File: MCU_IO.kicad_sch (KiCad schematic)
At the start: 44 parts, among them J15 Conn_01x02, Q1 IRLML2803, SW1 B3FS-1002P, SW2 B3FS-1002P, U1 RP235x-B, U2 MAX706RESA+, U3 MR25H40MDF, Y1 12MHz

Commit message: Addressed design issues
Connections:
- net Payload_EN: now also U1.37 (GPIO29); no longer U1.38 (GPIO30)
- net Payload_FLT: now also U1.38 (GPIO30); no longer U1.37 (GPIO29)

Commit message: v4.0 Updates
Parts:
- removed J15: Conn_01x02, Connector_PinHeader_2.54mm:PinHeader_1x02_P2.54mm_Vertical, symbol Connector_Generic:Conn_01x02
- added R13, R14, R15, R16: 100k, Resistor_SMD:R_0603_1608Metric, symbol Device:R_Small
- added TP1, TP2: TestPoint, TestPoint:TestPoint_Pad_D1.5mm, symbol Connector:TestPoint
- Y1: value 12MHz -> ABM8-272-T3; Part ABM8-272-T3 -> 12MHz
- renumbered D12 to D1, L4 to L1, R8 to R10, R9 to R11, R10 to R12, R162 to R5, R5 to R6, R163 to R7, R6 to R8, R7 to R9
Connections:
- net COIL_EN: now also R13.1
- net GND: now also R13.2, R14.2, R15.2, R16.2
- net HEATER_ENABLE: now also R14.1
- net Jetson_EN: now also R15.1
- net RW_EN: now also R16.1
- net SWCLK: now also TP2.1
- net SWDIO: now also TP1.1
- net Payload_CSn: no longer names the net of U1.36 (GPIO28)
- net Payload_EN: no longer names the net of U1.37 (GPIO29)
- net Payload_FLT: no longer names the net of U1.38 (GPIO30)
- net Payload_IO0: no longer names the net of U1.18 (GPIO18)
- net Payload_IO1: no longer names the net of U1.17 (GPIO17)
- net Payload_IO2: no longer names the net of U1.16 (GPIO16)
- no-connect marks 6 -> 12
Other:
- moved on the sheet: C10, C21, C22, L1, Q1, R10, R11, R12, R8, R9, SW1, SW2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

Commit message: DFM updates
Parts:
- C1, C14, C15, C16, C19, C2, C20, C22, C3, C4, C5, C6, C7, C8, C9: MPN (none) -> C307348
- C10: MPN (none) -> C16193991
- C11, C12: MPN (none) -> C3861036
- C13: MPN (none) -> C386084
- C17, C18: MPN (none) -> C346205
- C21: MPN (none) -> C2214844
- D1: Flight WS2812B-B -> (none); MPN (none) -> C2890040; Manufacturer_Name Worldsemi -> (none); Manufacturer_Part_Number WS2812B-B -> (none); Proto WS2812B-B -> (none)
- L1: MPN (none) -> C42411119; Part AOTA-B201610S3R3-101-T -> (none)
- Q1: MPN (none) -> C2590
- R1: MPN (none) -> C844757
- R10, R11, R7: MPN (none) -> C2479067
- R12, R5: MPN (none) -> C2484712
- R13, R14, R15, R16, R9: MPN (none) -> C237792
- R2: MPN (none) -> C3029194
- R3, R4: MPN (none) -> C844545
- R6: MPN (none) -> C844915
- R8: DNI (none) -> DNI; now left out of the parts list
- SW1, SW2: value B3FS-1002P -> B3U-1000P; MPN (none) -> C231329
- TP1, TP2: now left out of the parts list
- U1: MPN (none) -> C42415655
- U2: MPN (none) -> C28380
- Y1: MPN (none) -> C20625731

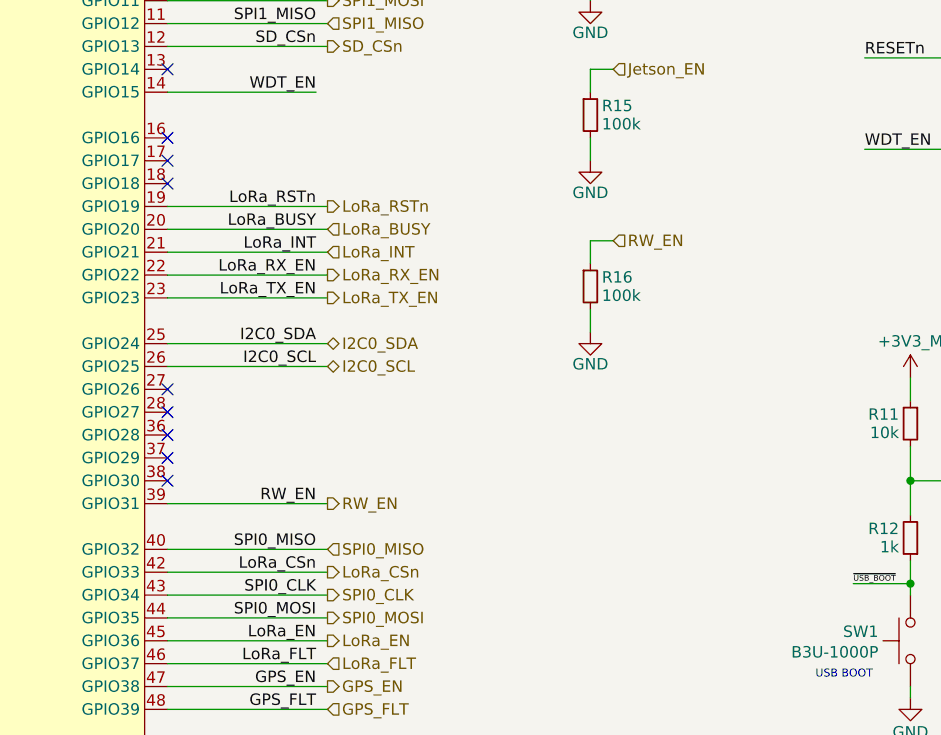
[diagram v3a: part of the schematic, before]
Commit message: Fixed Jetson FPC pinout
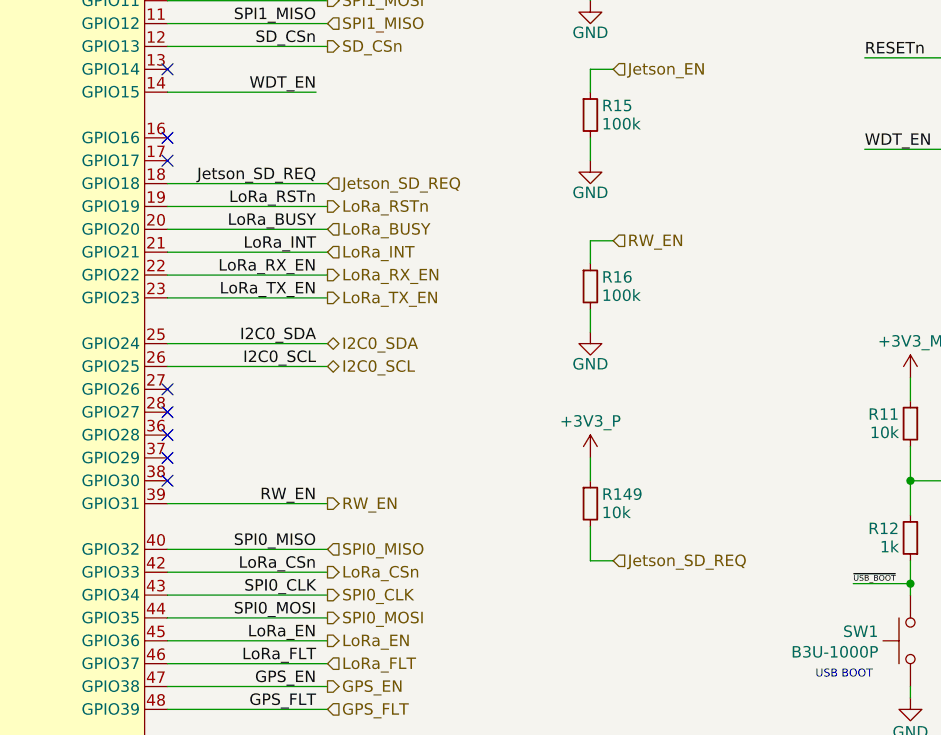
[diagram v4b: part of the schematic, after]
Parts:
- added R149: 10k, Resistor_SMD:R_0603_1608Metric, symbol Device:R_Small
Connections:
- net +3V3_P: now also R149.1
- net Jetson_SD_REQ: now reaches U1.18 (GPIO18)
- net Jetson_SD_REQ: now also R149.2
- no-connect marks 12 -> 11
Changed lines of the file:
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@@
 		(at 120.65 93.98)
 	)
-	(no_connect
-		(at 120.65 99.06)
-	)
 	(wire
 		(pts
@@
 	(wire
 		(pts
+			(xy 120.65 99.06) (xy 138.43 99.06)
+		)
+		(stroke
+			(width 0)
+			(type default)
+		)
+	)
+	(wire
+		(pts
 			(xy 68.58 66.04) (xy 68.58 68.58)
 		)
@@
 	(wire
 		(pts
+			(xy 167.64 137.16) (xy 167.64 140.97)
+		)
+		(stroke
+			(width 0)
+			(type default)
+		)
+	)
+	(wire
+		(pts
 			(xy 38.1 182.88) (xy 36.83 182.88)
 		)
@@
 	(wire
 		(pts
+			(xy 170.18 140.97) (xy 167.64 140.97)
+		)
+		(stroke
+			(width 0)
+			(type default)
+		)
+	)
+	(wire
+		(pts
 			(xy 54.61 144.78) (xy 44.45 144.78)
 		)
@@
 	(wire
 		(pts
+			(xy 167.64 132.08) (xy 167.64 129.54)
+		)
+		(stroke
+			(width 0)
+			(type default)
+		)
+	)
+	(wire
+		(pts
 			(xy 120.65 116.84) (xy 138.43 116.84)
 		)
@@
 		)
 	)
+	(label "Jetson_SD_REQ"
+		(at 137.16 99.06 180)
+		(effects
+			(font
+				(size 1.27 1.27)
+			)
+			(justify right bottom)
+		)
+	)
 	(label "Jetson_EN"
 		(at 137.16 66.04 180)
@@
 		)
 	)
+	(hierarchical_label "Jetson_SD_REQ"
+		(shape input)
+		(at 138.43 99.06 0)
+		(effects
+			(font
+				(size 1.27 1.27)
+			)
+			(justify left)
+		)
+	)
 	(hierarchical_label "3V3_P_FLT"
 		(shape input)
@@
 		)
 	)
+	(hierarchical_label "Jetson_SD_REQ"
+		(shape input)
+		(at 170.18 140.97 0)
+		(effects
+			(font
+				(size 1.27 1.27)
+			)
+			(justify left)
+		)
+	)
 	(hierarchical_label "UART0_RX"
 		(shape input)
@@
 	)
 	(symbol
+		(lib_id "power:+3V3")
+		(at 167.64 129.54 0)
+		(unit 1)
+		(exclude_from_sim no)
+		(in_bom yes)
+		(on_board yes)
+		(dnp no)
+		(property "Reference" "#PWR092"
+			(at 167.64 133.35 0)
+			(effects
+				(font
+					(size 1.27 1.27)
+				)
+				(hide yes)
+			)
+		)
+		(property "Value" "+3V3_P"
+			(at 167.64 125.476 0)
+			(effects
+				(font
+					(size 1.27 1.27)
+				)
+			)
+		)
+		(property "Footprint" ""
+			(at 167.64 129.54 0)
+			(effects
+				(font
+					(size 1.27 1.27)
+				)
+				(hide yes)
+			)
+		)
+		(property "Datasheet" ""
+			(at 167.64 129.54 0)
+			(effects
+				(font
+					(size 1.27 1.27)
+				)
+				(hide yes)
+			)
+		)
+		(property "Description" "Power symbol creates a global label with name \"+3V3\""
+			(at 167.64 129.54 0)
+			(effects
+				(font
+					(size 1.27 1.27)
+				)
+				(hide yes)
+			)
+		)
+		(pin "1"
+		)
+		(instances
+			(project "Avionics-MainBoard"
+				(path "/4c932743-8c6f-426e-9c1f-5a3f2b32c70d/21e71e76-dfb6-4af2-84cc-797c0fdddabe"
+					(reference "#PWR092")
+					(unit 1)
+				)
+			)
+		)
+	)
+	(symbol
 		(lib_id "Device:C_Small")
 		(at 251.46 95.25 0)
@@
 					(unit 1)
 				)
+			)
+		)
+	)
+	(symbol
+		(lib_id "Device:R_Small")
+		(at 167.64 134.62 0)
+		(unit 1)
+		(exclude_from_sim no)
+		(in_bom yes)
+		(on_board yes)
+		(dnp no)
+		(property "Reference" "R149"
+			(at 168.91 133.604 0)
+			(effects
+				(font
+					(size 1.27 1.27)
+				)
+				(justify left)
+			)
+		)
+		(property "Value" "10k"
+			(at 168.91 135.636 0)
+			(effects
+				(font
+					(size 1.27 1.27)
+				)
+				(justify left)
+			)
+		)
+		(property "Footprint" "Resistor_SMD:R_0603_1608Metric"
+			(at 167.64 134.62 0)
+			(effects
+				(font
+					(size 1.27 1.27)
+				)
+				(hide yes)
+			)
+		)
+		(property "Datasheet" "~"
+			(at 167.64 134.62 0)
+			(effects
+				(font
+					(size 1.27 1.27)
+				)
+				(hide yes)
+			)
+		)
+		(property "Description" "Resistor, small symbol"
+			(at 167.64 134.62 0)
+			(effects
+				(font
+					(size 1.27 1.27)
+				)
+				(hide yes)
+			)
+		)
+		(property "MPN" "C2479067"
+			(at 167.64 134.62 0)
+			(effects
+				(font
+					(size 1.27 1.27)
+				)
+				(hide yes)
+			)
+		)
+		(pin "2"
+		)
+		(pin "1"
+		)
+		(instances
+			(project "Avionics-MainBoard"
+				(path "/4c932743-8c6f-426e-9c1f-5a3f2b32c70d/21e71e76-dfb6-4af2-84cc-797c0fdddabe"
+					(reference "R149")
+					(unit 1)
+				)

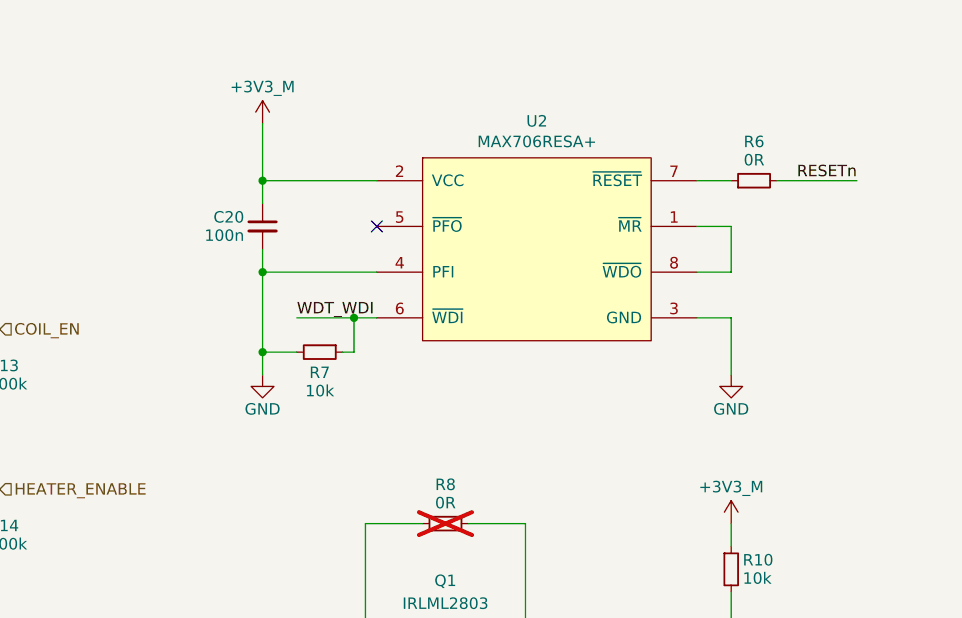
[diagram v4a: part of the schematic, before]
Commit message: updated watchdog
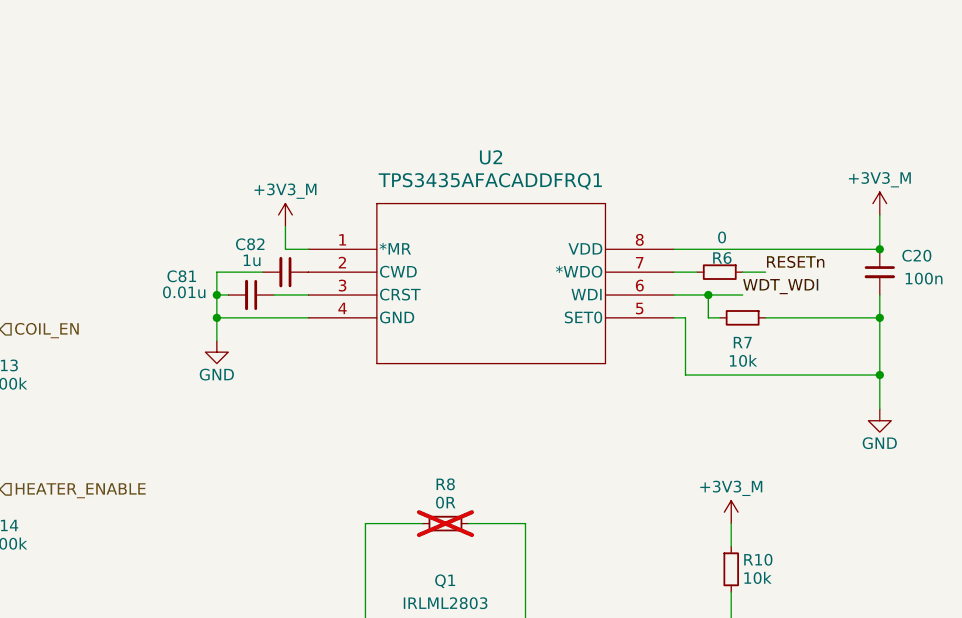
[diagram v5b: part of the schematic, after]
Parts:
- removed U2: MAX706RESA+, Package_SO:SOIC-8_3.9x4.9mm_P1.27mm, symbol Argus-IC:MAX706RESA+
- added C81: 0.01u, Capacitor_SMD:C_0603_1608Metric, symbol Device:C_Small
- added C82: 1u, Capacitor_SMD:C_0603_1608Metric, symbol Device:C_Small
- added U2: TPS3435AFACADDFRQ1, SOT23-8_DDF_TEX, symbol Argus-IC:TPS3435AFACADDFRQ1
- R6: value 0R -> 0; MPN C844915 -> C2479067
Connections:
- net +3V3_M: now also U2.1 (*MR), U2.8 (VDD)
- net GND: now also R7.1, C81.2, C82.2, U2.4 (GND), U2.5 (SET0); no longer R7.2
- net RESETn: now also R6.1; no longer R6.2
- net WDT_WDI: now also R7.2, U2.6 (WDI); no longer R7.1
- new net: C82.1, U2.2 (CWD)
- new net: C81.1, U2.3 (CRST)
- new net: R6.2, U2.7 (*WDO)
- no-connect marks 11 -> 10

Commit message: Updated WDT
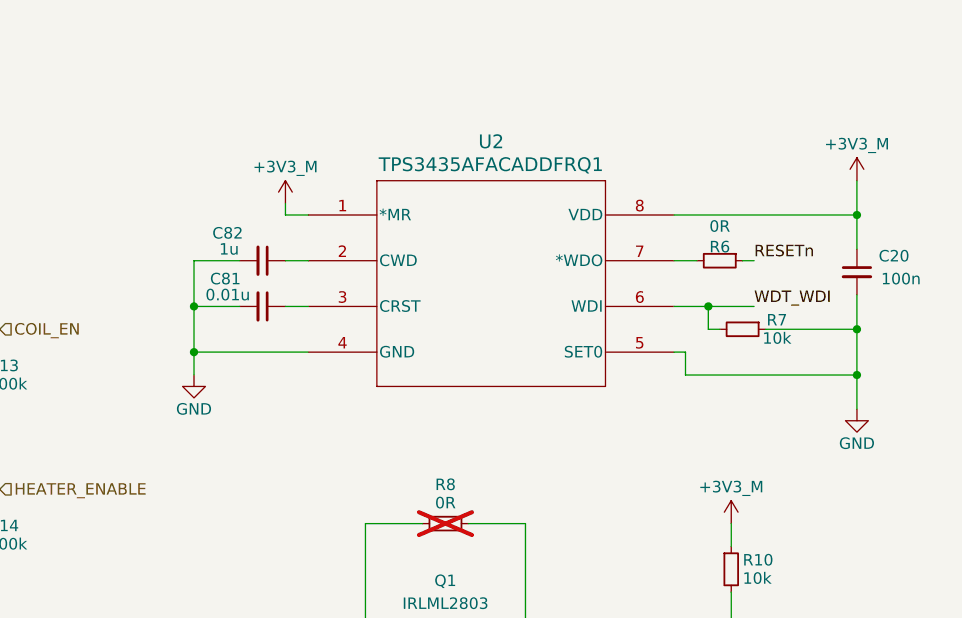
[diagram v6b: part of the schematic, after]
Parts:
- R6: value 0 -> 0R
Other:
- moved on the sheet: C20, C81, C82, R6, R7

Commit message: v4.2 Updates
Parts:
- C81: value 0.01u -> 10n
- U2: footprint SOT23-8_DDF_TEX -> Package_TO_SOT_SMD:TSOT-23-8
- U3: Alternate (none) -> W25Q32JVSNIQ
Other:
- moved on the sheet: C20, C81, C82, R6, R7
